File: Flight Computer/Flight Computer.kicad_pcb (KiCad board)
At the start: 2 copper layers, 58.5 x 77.5 mm, 1 part, among them IC1 ESP32-Wrover-IE-N16R8

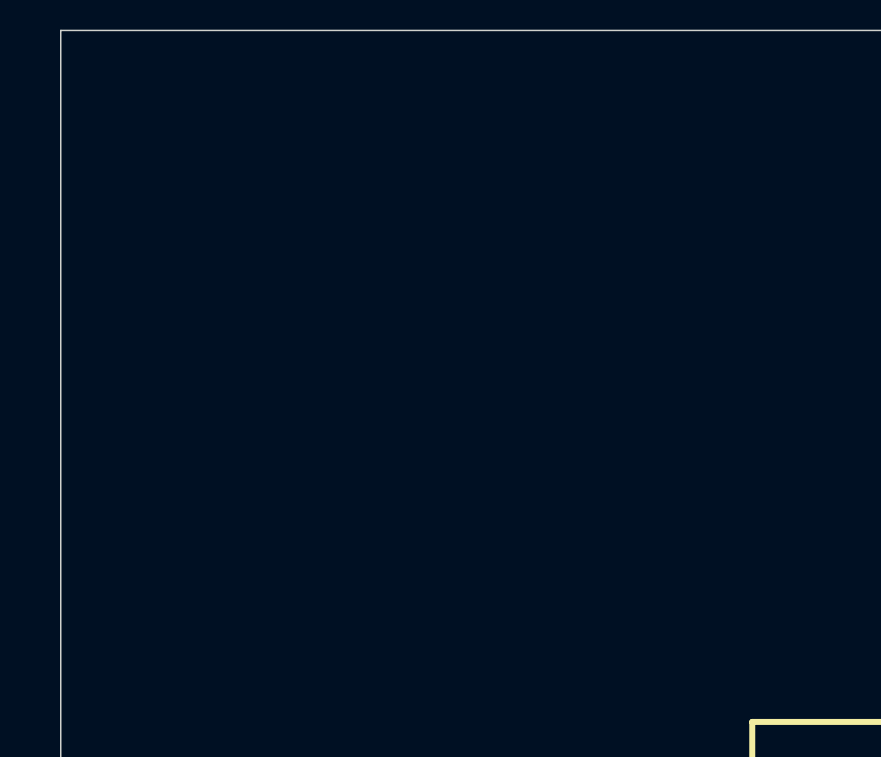
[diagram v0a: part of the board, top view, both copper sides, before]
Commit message: Added barometric pressure sensors and IMUs to footprint and symbol library
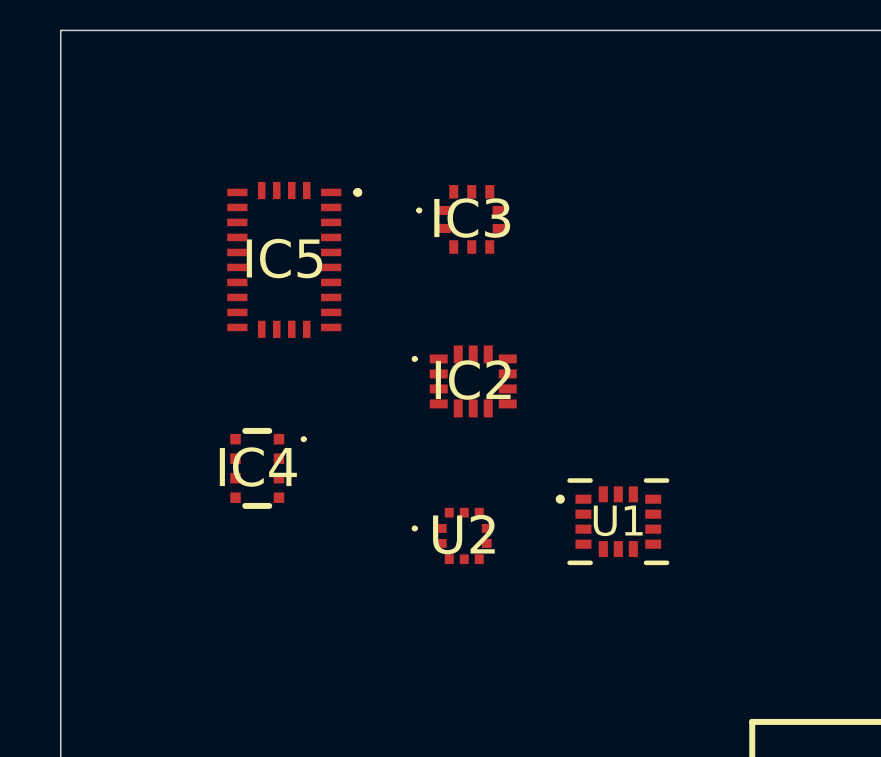
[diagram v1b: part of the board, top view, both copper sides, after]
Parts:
- added IC2: LSM6DSV16BXTR, Lander Electronics:LSM6DSV16BXTR, F.Cu at (115.8, 63.7)
- added IC3: LPS25HBTR, Lander Electronics:LPS25HBTR, F.Cu at (115.7, 58.3)
- added IC4: DPS368XTSA1, Lander Electronics:DPS368XTSA1, F.Cu at (108.5, 66.6)
- added IC5: BNO085, Lander Electronics:BNO085, F.Cu at (109.5, 59.6)
- added U1: ICM-45686, Lander Electronics:ICM45686, F.Cu at (120.6, 68.4)
- added U2: BMP581, Lander Electronics:BMP581, F.Cu at (115.5, 68.8)
